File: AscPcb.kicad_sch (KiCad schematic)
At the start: 64 parts, among them J1 12402012E212A, J2 B2B-PH-K-S(LF)(SN), J3 Conn_01x10_Pin, J4 Conn_01x06_Pin, J5 Screw_Terminal_01x02, J6 Conn_01x02_Pin, J7 Conn_01x02_Pin, J8 Conn_01x03_Pin, J9 Screw_Terminal_01x02, Q1 Q_NMOS_DGS, SW1 TL3305AF260QG, SW2 TL3305AF260QG, U1 ESP32-C3-WROOM-02-N4, U2 BQ24040DSQR, U3 TLV75801PDRVR, U5 LTC3625EDE_PBF, U8 AP62300TWU

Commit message: motor control circuit done
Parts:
- removed D5: D, symbol Device:D
- added D6: D_Schottky, Diode_SMD:D_SMA, symbol Device:D_Schottky
- J6, J7: footprint (none) -> Connector_PinHeader_2.54mm:PinHeader_1x02_P2.54mm_Vertical
- Q1: footprint (none) -> DMN1019USN-13:SC-59-pads-swapped; MPN (none) -> DMN1019USN-13
- renumbered z to U6
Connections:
- net +12V: now also D6.1 (K)
- net at J9.1 (Pin_1), Q1.1 (D): now also D6.2 (A)
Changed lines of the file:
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@@
 			)
 		)
-		(property "Footprint" ""
+		(property "Footprint" "Connector_PinHeader_2.54mm:PinHeader_1x02_P2.54mm_Vertical"
 			(at 364.49 160.02 0)
 			(effects
@@
 			)
 		)
-		(property "Footprint" ""
+		(property "Footprint" "DMN1019USN-13:SC-59-pads-swapped"
 			(at 137.16 44.45 0)
 			(effects
@@
 			)
 		)
-		(property "Datasheet" "~"
+		(property "Datasheet" "https://www.diodes.com/assets/Datasheets/DMN1019USN.pdf"
 			(at 134.62 39.37 0)
 			(effects
@@
 			)
 		)
+		(property "MPN" "DMN1019USN-13"
+			(at 134.62 39.37 90)
+			(effects
+				(font
+					(size 1.27 1.27)
+				)
+				(hide yes)
+			)
+		)
 		(pin "1"
 		)
@@
 	)
 	(symbol
-		(lib_id "Device:D")
-		(at 148.59 30.48 180)
-		(unit 1)
-		(exclude_from_sim no)
-		(in_bom yes)
-		(on_board yes)
-		(dnp no)
-		(fields_autoplaced yes)
-		(property "Reference" "D5"
-			(at 148.59 24.13 0)
-			(effects
-				(font
-					(size 1.27 1.27)
-				)
-			)
-		)
-		(property "Value" "D"
-			(at 148.59 26.67 0)
-			(effects
-				(font
-					(size 1.27 1.27)
-				)
-			)
-		)
-		(property "Footprint" ""
-			(at 148.59 30.48 0)
-			(effects
-				(font
-					(size 1.27 1.27)
-				)
-				(hide yes)
-			)
-		)
-		(property "Datasheet" "~"
-			(at 148.59 30.48 0)
-			(effects
-				(font
-					(size 1.27 1.27)
-				)
-				(hide yes)
-			)
-		)
-		(property "Description" "Diode"
-			(at 148.59 30.48 0)
-			(effects
-				(font
-					(size 1.27 1.27)
-				)
-				(hide yes)
-			)
-		)
-		(property "Sim.Device" "D"
-			(at 148.59 30.48 0)
-			(effects
-				(font
-					(size 1.27 1.27)
-				)
-				(hide yes)
-			)
-		)
-		(property "Sim.Pins" "1=K 2=A"
-			(at 148.59 30.48 0)
-			(effects
-				(font
-					(size 1.27 1.27)
-				)
-				(hide yes)
-			)
-		)
-		(pin "2"
-		)
-		(pin "1"
-		)
-		(instances
-			(project ""
-				(path "/15a81d81-777d-4164-ac7f-1386d28fdd79"
-					(reference "D5")
-					(unit 1)
-				)
-			)
-		)
-	)
-	(symbol
 		(lib_id "power:+12V")
 		(at 156.21 41.91 270)
@@
 			)
 		)
-		(property "Footprint" ""
+		(property "Footprint" "Connector_PinHeader_2.54mm:PinHeader_1x02_P2.54mm_Vertical"
 			(at 121.92 146.05 0)
 			(effects
@@
 	)
 	(symbol
+		(lib_id "Device:D_Schottky")
+		(at 148.59 30.48 180)
+		(unit 1)
+		(exclude_from_sim no)
+		(in_bom yes)
+		(on_board yes)
+		(dnp no)
+		(fields_autoplaced yes)
+		(property "Reference" "D6"
+			(at 148.9075 24.13 0)
+			(effects
+				(font
+					(size 1.27 1.27)
+				)
+			)
+		)
+		(property "Value" "D_Schottky"
+			(at 148.9075 26.67 0)
+			(effects
+				(font
+					(size 1.27 1.27)
+				)
+			)
+		)
+		(property "Footprint" "Diode_SMD:D_SMA"
+			(at 148.59 30.48 0)
+			(effects
+				(font
+					(size 1.27 1.27)
+				)
+				(hide yes)
+			)
+		)
+		(property "Datasheet" "https://www.diodes.com/assets/Datasheets/B220_A-B260_A.pdf"
+			(at 148.59 30.48 0)
+			(effects
+				(font
+					(size 1.27 1.27)
+				)
+				(hide yes)
+			)
+		)
+		(property "Description" "Schottky diode"
+			(at 148.59 30.48 0)
+			(effects
+				(font
+					(size 1.27 1.27)
+				)
+				(hide yes)
+			)
+		)
+		(property "MPN" "B240A-13-F"
+			(at 148.59 30.48 0)
+			(effects
+				(font
+					(size 1.27 1.27)
+				)
+				(hide yes)
+			)
+		)
+		(pin "1"
+		)
+		(pin "2"
+		)
+		(instances
+			(project ""
+				(path "/15a81d81-777d-4164-ac7f-1386d28fdd79"
+					(reference "D6")
+					(unit 1)
+				)
+			)
+		)
+	)
+	(symbol
 		(lib_id "Connector:Conn_01x06_Pin")
 		(at 44.45 267.97 0)
@@
 		(dnp no)
 		(fields_autoplaced yes)
-		(property "Reference" "z"
+		(property "Reference" "U6"
 			(at 64.77 212.09 0)
 			(effects
@@
 			(project ""
 				(path "/15a81d81-777d-4164-ac7f-1386d28fdd79"
-					(reference "z")
+					(reference "U6")
 					(unit 1)
 				)

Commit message: usb to serial converter, some safety features and monitoring
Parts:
- removed J3: Conn_01x10_Pin, Connector_PinHeader_2.54mm:PinHeader_1x10_P2.54mm_Vertical, symbol Connector:Conn_01x10_Pin
- added C17, C18: 100nF, Capacitor_SMD:C_0603_1608Metric, symbol Device:C
- added C19: 4.7uF, Capacitor_SMD:C_0603_1608Metric, symbol Device:C
- added D5: D_Schottky, Diode_SMD:D_SMA, symbol Device:D_Schottky
- added J10, J11, J12, J14, J15, J16, J3: Conn_01x02_Pin, Connector_PinHeader_2.54mm:PinHeader_1x02_P2.54mm_Vertical, symbol Connector:Conn_01x02_Pin
- added J13: Conn_01x12_Pin, Connector_PinHeader_2.54mm:PinHeader_1x12_P2.54mm_Vertical, symbol Connector:Conn_01x12_Pin
- added Q4, Q5: BC817, Package_TO_SOT_SMD:SOT-23, symbol Transistor_BJT:BC817
- added R19, R20, R22, R23, R24: 10k, Resistor_SMD:R_0603_1608Metric, symbol Device:R
- added R21: 1k, Resistor_SMD:R_0603_1608Metric, symbol Device:R
- added U4: CP2102N-A02-GQFN24R, CP2102N-A02-GQFN24R:QFN50P400X400X80-25N, symbol CP2102N-A02-GQFN24R:CP2102N-A02-GQFN24R
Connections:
- net SA0 is gone; now on net GND: U6.1 (SDO)
- net +5V: now also D5.1 (K), J10.2 (Pin_2); no longer J1.A4_B9 (VBUS), J1.B4_A9 (VBUS__1)
- net D+: now also J11.2 (Pin_2), J14.2 (Pin_2); no longer U1.14 (IO19)
- net D-: now also J12.2 (Pin_2), J3.2 (Pin_2); no longer U1.13 (IO18)
- net GND: now also C17.1, C18.1, C19.1, R22.2, R24.2, U4.2 (GND), U4.25 (GND__1)
- net IO0: now also J13.1 (Pin_1)
- net IO1: now also J13.2 (Pin_2)
- net IO10: now also J13.8 (Pin_8)
- net IO3: now also J13.3 (Pin_3), R21.2, R22.1; no longer Q1.2 (G)
- net IO4: now also J13.4 (Pin_4), R23.1, R24.1
- net IO5: now also J13.5 (Pin_5)
- net IO6: now also J13.6 (Pin_6)
- net IO7: now also J13.7 (Pin_7)
- net POWER: now also R23.2
- net IO9: now reaches C8.1, R10.2, SW2.3, SW2.4, U1.8 (IO9)
- net IO9: now also Q4.3 (C)
- net EN: now reaches C7.1, R9.2, SW1.3, SW1.4, U1.2 (EN)
- net EN: now also Q5.3 (C)
- net IO20 renamed ESP_RXD
- net ESP_RXD: now also J13.12 (Pin_12), J16.2 (Pin_2)
- net IO21 renamed ESP_TXD
- net ESP_TXD: now also J13.11 (Pin_11), J15.2 (Pin_2)
- new net: Q4.1 (B), R20.2
- new net: C18.2, C19.2, J10.1 (Pin_1), U4.7 (VREGIN), U4.8 (VBUS)
- new net: Q5.1 (B), R19.2
- new net: C17.2, U4.6 (VDD)
- new net: D5.2 (A), J1.A4_B9 (VBUS), J1.B4_A9 (VBUS__1)
- new net: Q1.2 (G), R21.1
- new net: J12.1 (Pin_1), U4.4 (D-)
- new net: J16.1 (Pin_1), U4.21 (TXD)
- new net: J15.1 (Pin_1), U4.20 (RXD)
- new net: J11.1 (Pin_1), U4.3 (D+)
- new net DTR: Q4.2 (E), R19.1, U4.23 (~{DTR})
- new net IO18: J13.9 (Pin_9), J3.1 (Pin_1), U1.13 (IO18)
- new net IO19: J13.10 (Pin_10), J14.1 (Pin_1), U1.14 (IO19)
- new net RTS: Q5.2 (E), R20.1, U4.19 (~{RTS})
- no-connect marks 9 -> 21
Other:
- moved on the sheet: C5, C6

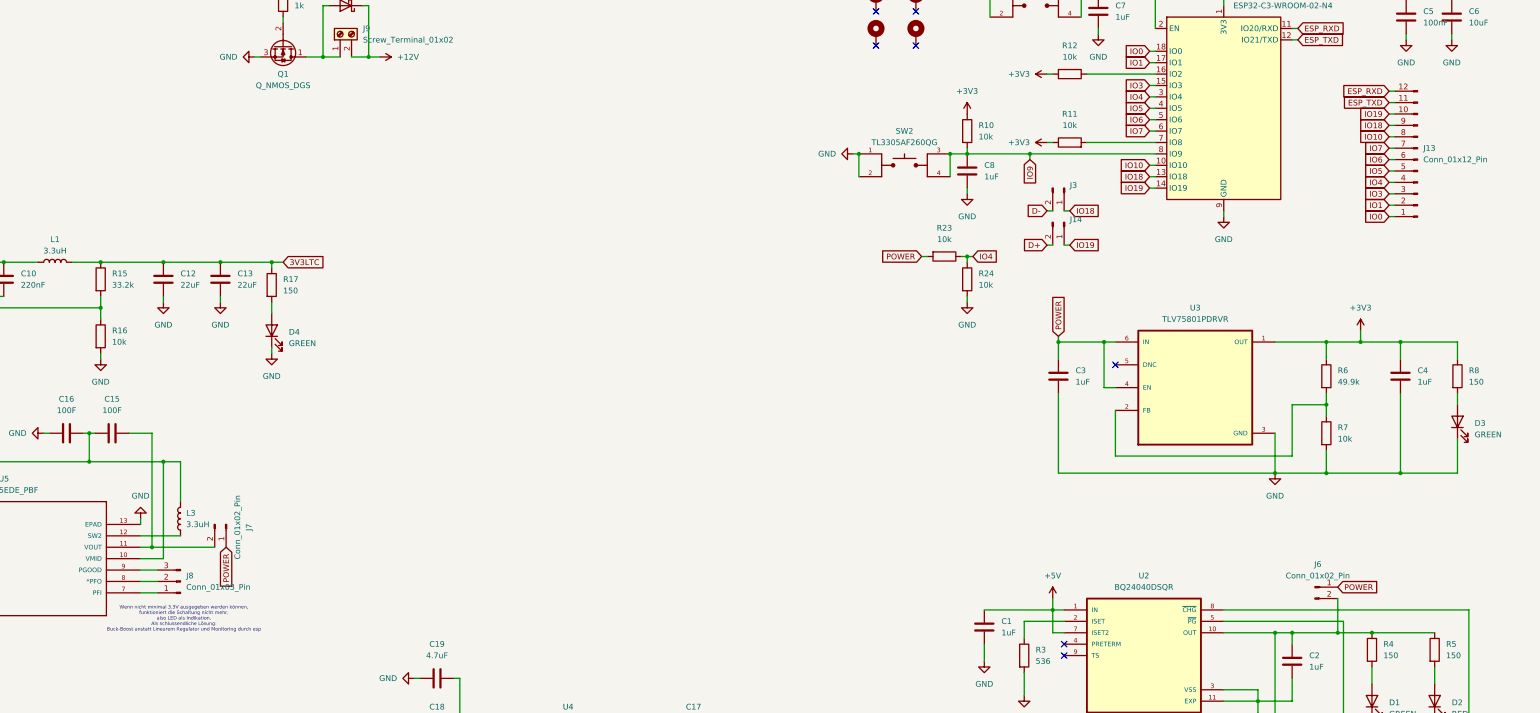
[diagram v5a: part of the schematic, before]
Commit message: add schmitt trigger
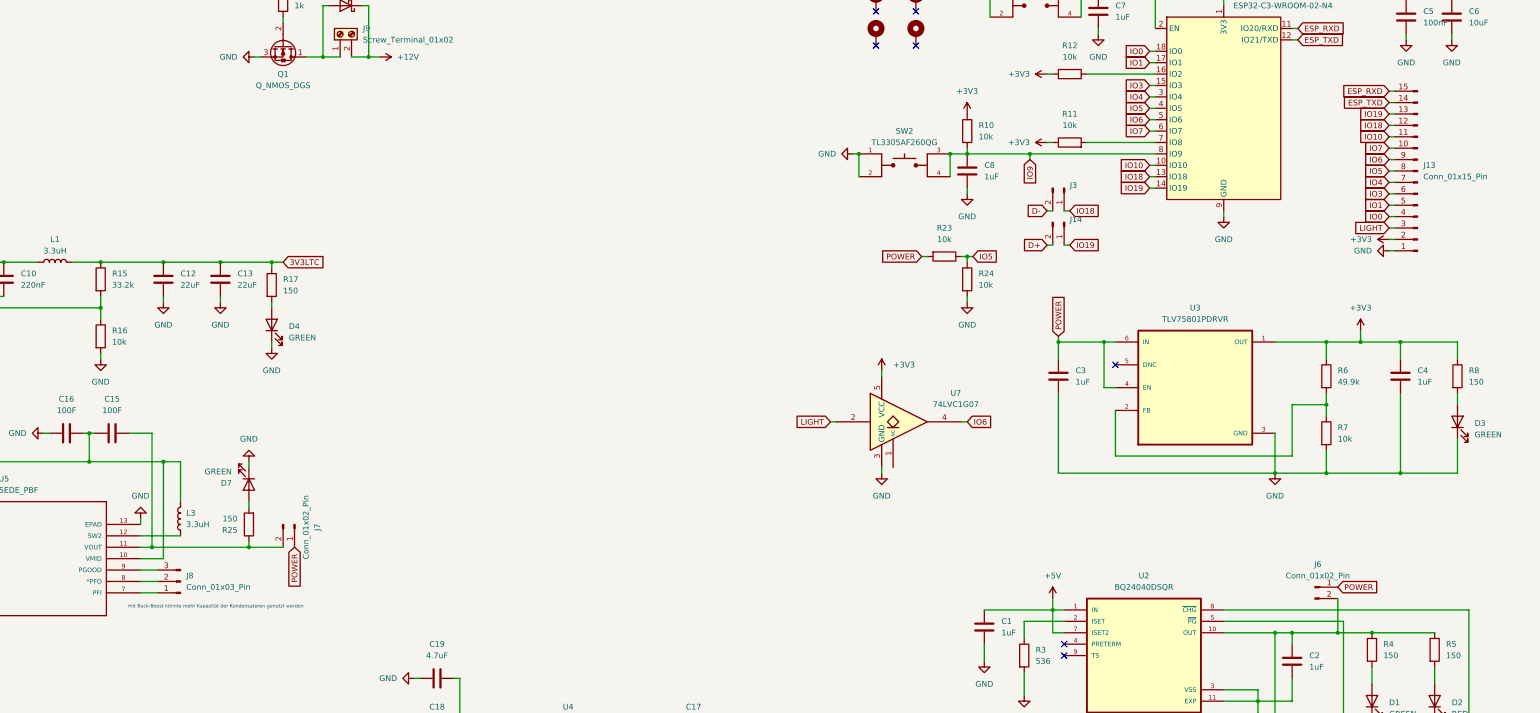
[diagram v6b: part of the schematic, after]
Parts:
- removed J13: Conn_01x12_Pin, Connector_PinHeader_2.54mm:PinHeader_1x12_P2.54mm_Vertical, symbol Connector:Conn_01x12_Pin
- added D7: GREEN, LED_SMD:LED_0603_1608Metric, symbol Device:LED
- added J13: Conn_01x15_Pin, symbol Connector:Conn_01x15_Pin
- added R25: 150, Resistor_SMD:R_0603_1608Metric, symbol Device:R
- added U7: 74LVC1G07, Package_TO_SOT_SMD:SOT-353_SC-70-5, symbol 74xGxx:74LVC1G07
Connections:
- net +3V3: now also J13.2 (Pin_2), U7.5 (VCC)
- net ESP_RXD: now also J13.15 (Pin_15)
- net ESP_TXD: now also J13.14 (Pin_14)
- net GND: now also D7.1 (K), J13.1 (Pin_1), U7.3 (GND)
- net IO0: now also J13.4 (Pin_4)
- net IO1: now also J13.5 (Pin_5)
- net IO10: now also J13.11 (Pin_11)
- net IO18: now also J13.12 (Pin_12)
- net IO19: now also J13.13 (Pin_13)
- net IO3: now also J13.6 (Pin_6)
- net IO4: now also J13.7 (Pin_7); no longer R23.1, R24.1
- net IO5: now also R23.1, R24.1, J13.8 (Pin_8)
- net IO6: now also J13.9 (Pin_9), U7.4
- net IO7: now also J13.10 (Pin_10)
- net at C15.2, J7.2 (Pin_2), U5.11 (VOUT): now also R25.1
- new net: D7.2 (A), R25.2
- new net LIGHT: J13.3 (Pin_3), U7.2
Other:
- note added: "mit Buck-Boost könnte mehr Kapazität der Kondensatoren genutzt werden"
- note removed: "Wenn nicht minimal 3.3V ausgegeben werden können, funktioniert die Schaltung nicht mehr, also LED als Indikation. Als schlussendliche Lösung: Buck-Boost anstatt Linearem Regulator und Monitoring durch esp"
- moved on the sheet: D4, J7

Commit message: bq24 according to datasheet, also fix cp2102, fix naming
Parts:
- added C19: 4.7uF, Capacitor_SMD:C_0603_1608Metric, symbol Device:C
- added R22: 22.1k, Resistor_SMD:R_0603_1608Metric, symbol Device:R
- added R23: 47.5k, Resistor_SMD:R_0603_1608Metric, symbol Device:R
- added R4: 2k, Resistor_SMD:R_0603_1608Metric, symbol Device:R
- added R5: 10k, Resistor_SMD:R_0603_1608Metric, symbol Device:R
- R3: value 536 -> 1k; MPN ERJ-3EKF5360V -> CRCW06031K00FKEA
- R6: renamed from R4; value 150 -> 1.5k; MPN CRCW0603150RFKEAC -> RC0603JR-071K5L
- R7: renamed from R5; value 150 -> 1.5k; MPN CRCW0603150RFKEAC -> RC0603JR-071K5L
- renumbered C15 to C10, C16 to C11, C5 to C12, C6 to C13, C7 to C14, C8 to C15, C18 to C16, C19 to C17, C17 to C18, C11 to C20, C9 to C5, C10 to C6, C12 to C7, C13 to C8, C14 to C9, D5 to D1, D1 to D2, D2 to D3, D3 to D4, D4 to D5, D7 to D6, D6 to D7, J15 to J13, J16 to J14, J3 to J15, J14 to J16, J5 to J3, J9 to J4, J13 to J5, J4 to J6, J6 to J7, J7 to J8, J8 to J9, Q5 to Q2, Q4 to Q3, R8 to R10, R15 to R11, R16 to R12, R17 to R13, R18 to R14, R25 to R15, R9 to R16, R12 to R17, R11 to R18, R10 to R19, R23 to R20, R24 to R21, R19 to R24, R20 to R25, R14 to R26, R13 to R27, R22 to R28, R21 to R29, R6 to R8, R7 to R9, U2 to U1, U3 to U2, U8 to U3, U5 to U4, U1 to U5, U4 to U6, U6 to U7, U7 to U8
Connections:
- net +5V: now also C1.2, R22.2; no longer C1.1, J10.2 (Pin_2)
- net GND: now also C1.1, R3.1, C19.2, R23.2, R4.1, R5.1; no longer C1.2, R3.2
- net at C18.2, U6.6 (VDD): now also U6.5 (VIO), C19.1
- net at U1.2 (ISET): now also R3.2; no longer R3.1
- net at U1.4 (PRETERM): now also R4.2
- net at U1.9 (TS): now also R5.2
- new net: J10.2 (Pin_2), R22.1, R23.1
- no-connect marks 21 -> 18
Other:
- moved on the sheet: C18

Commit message: double checked everything in schematic
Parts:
- removed J9: Conn_01x03_Pin, Connector_PinHeader_2.54mm:PinHeader_1x03_P2.54mm_Vertical, symbol Connector:Conn_01x03_Pin
- added J17: Conn_01x02_Pin, Connector_PinHeader_2.54mm:PinHeader_1x02_P2.54mm_Vertical, symbol Connector:Conn_01x02_Pin
- L1: footprint Inductor_SMD:L_0805_2012Metric -> DR73-3R3-R:DR73-3R3-R_EAT; MPN MLZ2012M3R3ATD69 -> DR73-3R3-R
- L2, L3: MPN DR73-3R3-R -> DR73-3R3-R
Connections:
- net 3V3LTC: now also J17.2 (Pin_2); no longer C9.2, U4.2 (VIN), U4.5 (EN)
- net at U4.7 (PFI): now also C9.2, U4.2 (VIN), U4.5 (EN), J17.1 (Pin_1)
- no-connect marks 18 -> 20
